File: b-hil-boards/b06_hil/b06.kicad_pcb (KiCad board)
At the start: 2 copper layers, 100 x 50 mm, 22 parts, among them J1 Conn_01x08_Socket, J3 USB_C_Receptacle_PowerOnly_6P, SW1 SW_Push, U4 ESP32_C3_SuperMini, U5 OLED-128x64-I2C

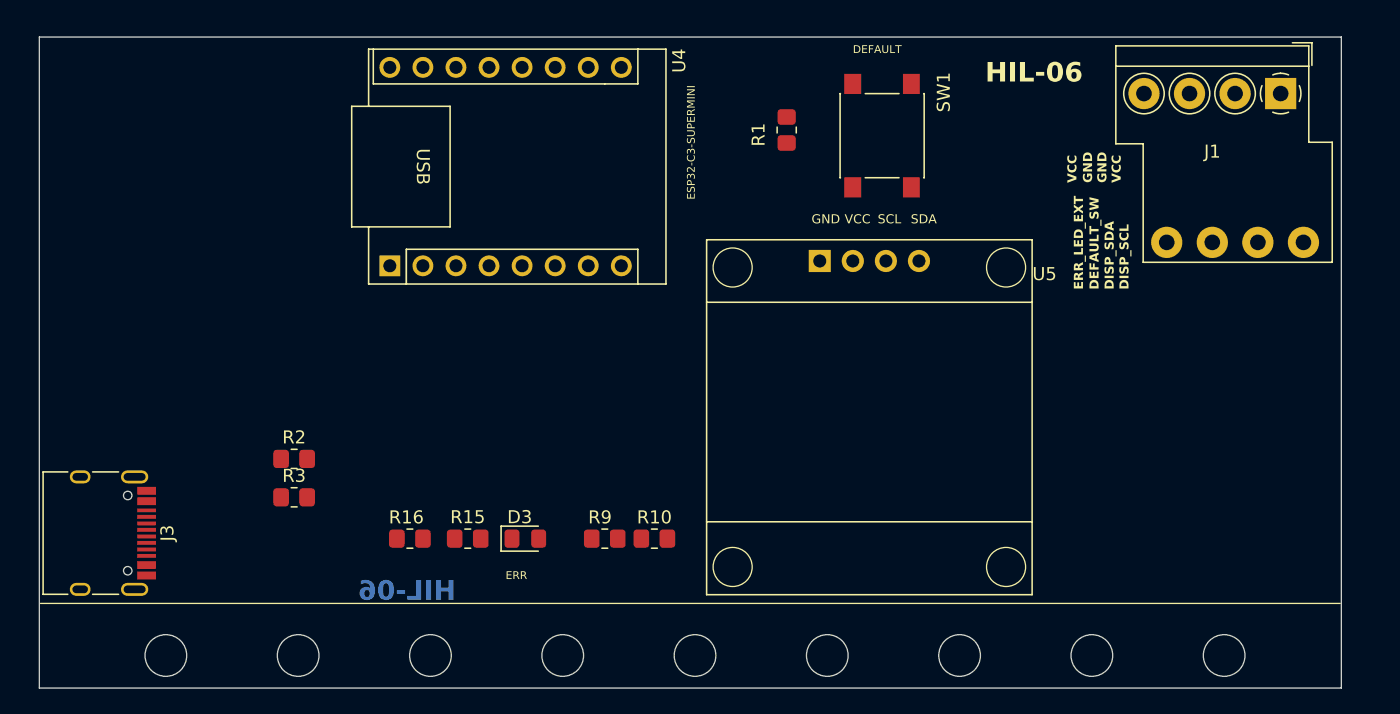
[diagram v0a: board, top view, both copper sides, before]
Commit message: B06: finalize PCB routing and design data
Complete the routed layout in b06.kicad_pcb, align schematic and project
settings, refresh fp-info-cache and sym-lib-table, add FreeRouting exchange
files (b06.dsn, b06.rules, b06.ses), the INA219 datasheet asset, the
Connector_Improved library symbol, and KiCad automatic backup archives.
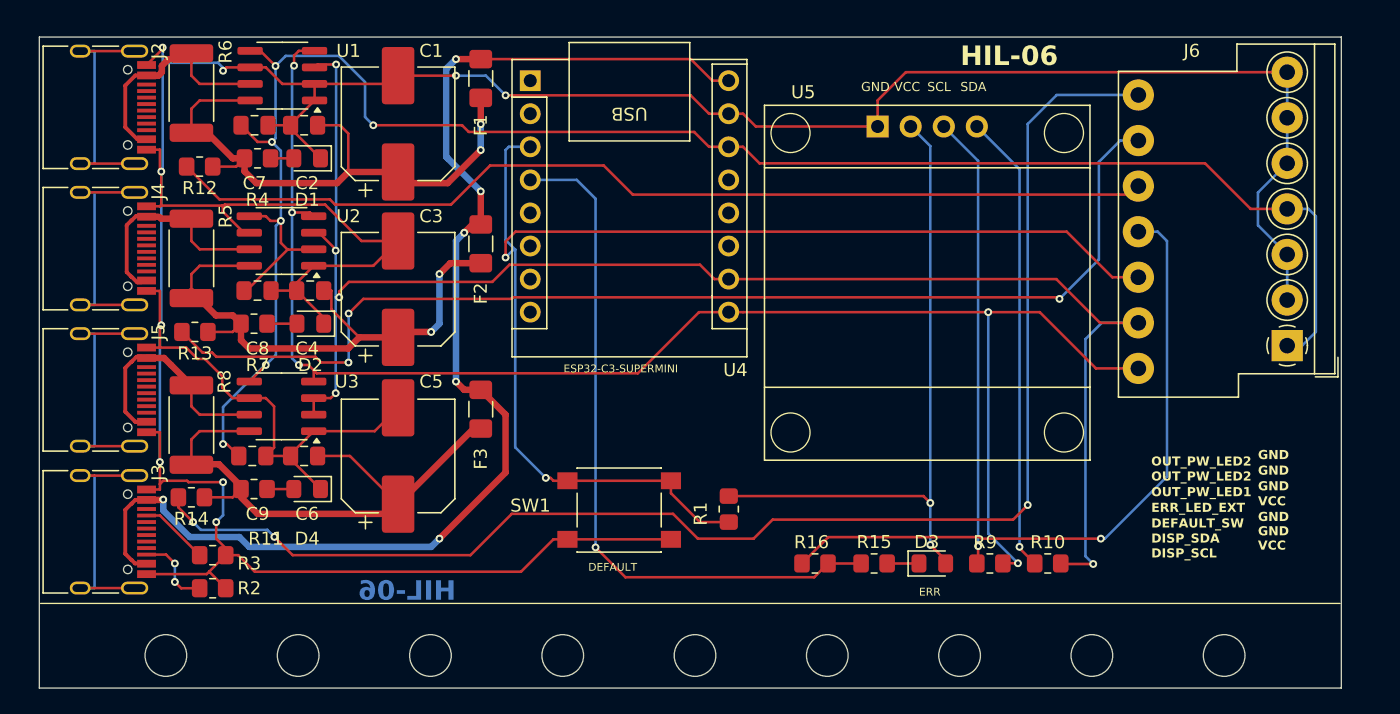
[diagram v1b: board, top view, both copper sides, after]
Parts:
- removed J1: Conn_01x08_Socket, TerminalBlock_DoubleLevel:TerminalBlock_DoubleLevel_2x04_P3.50mm_Horizontal
- added C1: C, Capacitor_SMD:CP_Elec_8x10.5, F.Cu at (107.3, 41.2)
- added C2: C, Capacitor_SMD:C_0805_2012Metric_Pad1.18x1.45mm_HandSolder, F.Cu at (100.1, 41.3)
- added C3: C, Capacitor_SMD:CP_Elec_8x10.5, F.Cu at (107.3, 53.9)
- added C4: C, Capacitor_SMD:C_0805_2012Metric_Pad1.18x1.45mm_HandSolder, F.Cu at (100.6, 54.0)
- added C5: C, Capacitor_SMD:CP_Elec_8x10.5, F.Cu at (107.3, 66.7)
- added C6: C, Capacitor_SMD:C_0805_2012Metric_Pad1.18x1.45mm_HandSolder, F.Cu at (100.1, 66.7)
- added C7: C, Capacitor_SMD:C_0805_2012Metric_Pad1.18x1.45mm_HandSolder, F.Cu at (96.3, 41.3)
- added C8: C, Capacitor_SMD:C_0805_2012Metric_Pad1.18x1.45mm_HandSolder, F.Cu at (96.5, 54.0)
- added C9: C, Capacitor_SMD:C_0805_2012Metric_Pad1.18x1.45mm_HandSolder, F.Cu at (96.1, 66.7)
- added D1: LED, LED_SMD:LED_0805_2012Metric_Pad1.15x1.40mm_HandSolder, F.Cu at (100.3, 43.8)
- added D2: LED, LED_SMD:LED_0805_2012Metric_Pad1.15x1.40mm_HandSolder, F.Cu at (100.6, 56.5)
- added D4: LED, LED_SMD:LED_0805_2012Metric_Pad1.15x1.40mm_HandSolder, F.Cu at (100.3, 69.2)
- added F1: Polyfuse, Fuse:Fuse_1206_3216Metric_Pad1.42x1.75mm_HandSolder, F.Cu at (113.7, 37.7)
- added F2: Polyfuse, Fuse:Fuse_1206_3216Metric_Pad1.42x1.75mm_HandSolder, F.Cu at (113.7, 50.4)
- added F3: Polyfuse, Fuse:Fuse_1206_3216Metric_Pad1.42x1.75mm_HandSolder, F.Cu at (113.7, 63.1)
- added J2: USB_C_Receptacle_PowerOnly_6P_Improved, Connector_USB:USB_C_Receptacle_HRO_TYPE-C-31-M-12, F.Cu at (84.0, 39.9)
- added J4: USB_C_Receptacle_PowerOnly_6P_Improved, Connector_USB:USB_C_Receptacle_HRO_TYPE-C-31-M-12, F.Cu at (84.0, 50.8)
- added J5: USB_C_Receptacle_PowerOnly_6P_Improved, Connector_USB:USB_C_Receptacle_HRO_TYPE-C-31-M-12, F.Cu at (84.0, 61.6)
- added J6: Conn_01x14_Socket, TerminalBlock_DoubleLevel:TerminalBlock_DoubleLevel_2x07_P3.50mm_Horizontal, F.Cu at (175.6, 58.2)
- added R11: R, Resistor_SMD:R_0805_2012Metric_Pad1.20x1.40mm_HandSolder, F.Cu at (96.2, 69.2)
- added R12: R, Resistor_SMD:R_0805_2012Metric_Pad1.20x1.40mm_HandSolder, F.Cu at (92.1, 44.5)
- added R13: R, Resistor_SMD:R_0805_2012Metric_Pad1.20x1.40mm_HandSolder, F.Cu at (91.7, 57.1)
- added R14: R, Resistor_SMD:R_0805_2012Metric_Pad1.20x1.40mm_HandSolder, F.Cu at (91.4, 69.8)
- added R4: R, Resistor_SMD:R_0805_2012Metric_Pad1.20x1.40mm_HandSolder, F.Cu at (96.5, 43.8)
- added R5: R, Resistor_SMD:R_2512_6332Metric_Pad1.40x3.35mm_HandSolder, F.Cu at (91.4, 51.5)
- added R6: R, Resistor_SMD:R_2512_6332Metric_Pad1.40x3.35mm_HandSolder, F.Cu at (91.4, 38.8)
- added R7: R, Resistor_SMD:R_0805_2012Metric_Pad1.20x1.40mm_HandSolder, F.Cu at (96.2, 56.5)
- added R8: R, Resistor_SMD:R_2512_6332Metric_Pad1.40x3.35mm_HandSolder, F.Cu at (91.4, 64.3)
- added U1: INA219AxD, Package_SO:SOIC-8_3.9x4.9mm_P1.27mm, F.Cu at (98.4, 37.5)
- added U2: INA219AxD, Package_SO:SOIC-8_3.9x4.9mm_P1.27mm, F.Cu at (98.4, 50.2)
- added U3: INA219AxD, Package_SO:SOIC-8_3.9x4.9mm_P1.27mm, F.Cu at (98.4, 62.9)
- J3: value USB_C_Receptacle_PowerOnly_6P -> USB_C_Receptacle_PowerOnly_6P_Improved
- moved SW1 35.1 mm to (124.3, 70.8), turned to 0 degrees
- moved D3 31.3 mm to (148.3, 74.9)
- moved R15 31.3 mm to (143.9, 74.9)
- moved R16 31.2 mm to (139.3, 74.9)
- moved R10 30.3 mm to (157.2, 74.9)
- moved R9 29.6 mm to (152.8, 74.9)
- moved R1 29.5 mm to (132.7, 70.8)
- moved U4 17.8 mm to (117.5, 37.9), turned to 180 degrees
- moved R2 11.7 mm to (93.1, 76.8)
- moved U5 11.2 mm to (144.1, 41.4)
- moved R3 7.67 mm to (93.1, 74.3)
- moved J3 0.10 mm to (84.0, 72.5)
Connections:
- J3 pad A1: (no net) -> GND
- J3 pad A12: GND1 -> GND
- J3 pad A4: (no net) -> +5V
- J3 pad B1: (no net) -> GND
- J3 pad B12: GND1 -> GND
- J3 pad B4: (no net) -> +5V
- R2 pad 2: GND1 -> GND
- R3 pad 2: GND1 -> GND
- SW1 pad 2: GND1 -> GND
- U4 pad 14: unconnected-(U4-3V3-Pad14) -> +3.3V
- U4 pad 15: GND1 -> GND
- U5 pad 1: GND1 -> GND
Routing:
- net GND: track 0.00 -> 298.0 mm, vias 0 -> 9
- net +3.3V: track 0.00 -> 150.4 mm, vias 0 -> 6
- net /DISP_SDA: track 0.00 -> 121.8 mm, vias 0 -> 5
- net /DISP_SCL: track 0.00 -> 118.8 mm, vias 0 -> 5
- net /OUT_PW_LED3: track 0.00 -> 109.5 mm, vias 0 -> 3
- net /DEFAULTS: track 0.00 -> 97.1 mm, vias 0 -> 2
- net +5V: track 0.00 -> 97.0 mm, vias 0 -> 6
- net /OUT_PW_LED2: track 0.00 -> 88.2 mm, vias 0 -> 3
- net /OUT_PW_LED1: track 0.00 -> 76.7 mm
- net /ERR_LED: track 0.00 -> 54.2 mm, vias 0 -> 1
- net /ERR_LED_EXT: track 0.00 -> 51.5 mm, vias 0 -> 1
- net +3V3: track 0.00 -> 50.4 mm, vias 0 -> 2
- net Net-(U2-IN+): track 0.00 -> 45.7 mm, vias 0 -> 2
- net Net-(U1-IN+): track 0.00 -> 45.0 mm, vias 0 -> 2
- net Net-(U3-IN+): track 0.00 -> 43.2 mm
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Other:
- board text added: "OUT_PW_LED1"
- board text added: "OUT_PW_LED2"
- board text added: "OUT_PW_LED3"

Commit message: B06: add single-board Gerber outputs
Export gerber/single (copper, mask, paste, silkscreen, edge cuts, drills, and b06-single.zip) for one-up fabrication; refresh PCB, schematic, and project layout; rotate KiCad automatic backups.
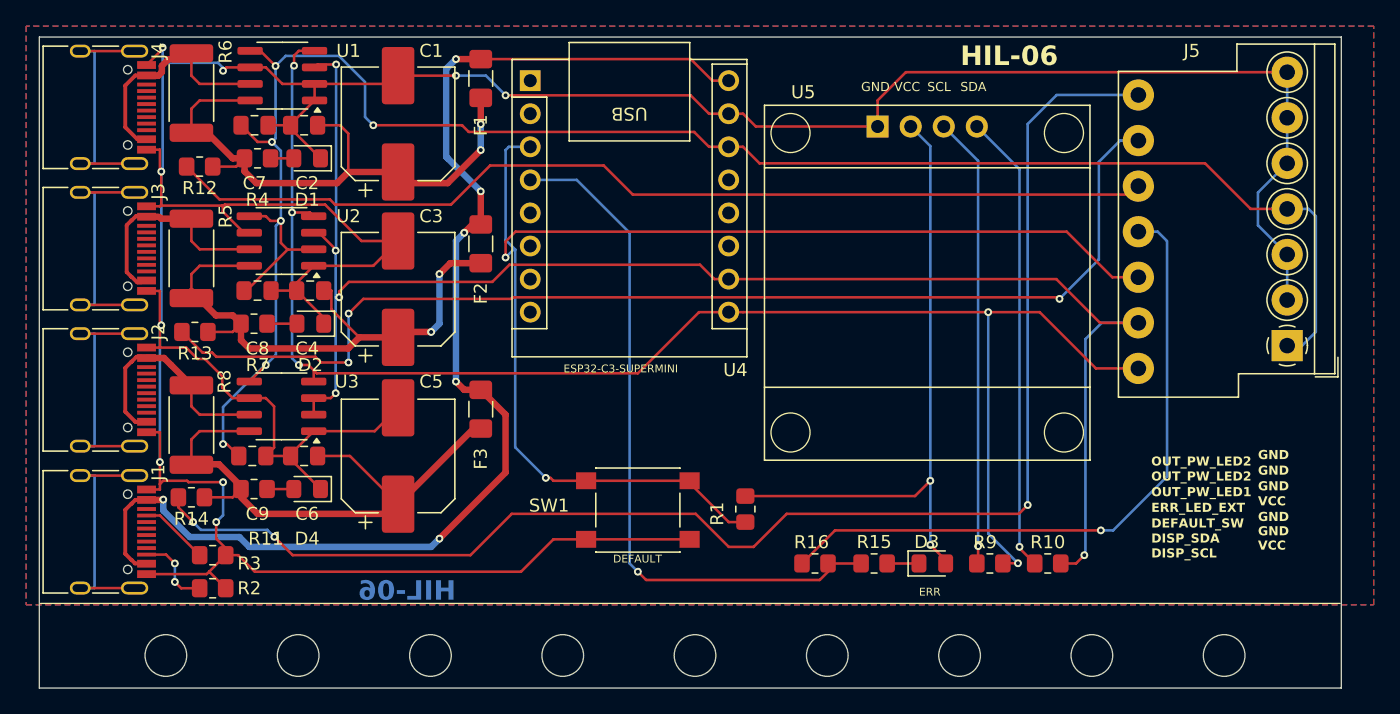
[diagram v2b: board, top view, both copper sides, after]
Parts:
- moved SW1 1.44 mm to (125.7, 70.8)
- moved R1 1.27 mm to (134.0, 70.8)
- renumbered J3 to J1, J5 to J2, J4 to J3, J2 to J4, J6 to J5
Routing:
- net GND: track 298.0 -> 299.5 mm
- net /DISP_SDA: track 121.8 -> 120.5 mm
- net +3V3: track 50.4 -> 49.4 mm
- net /DEFAULTS: track 97.1 -> 97.9 mm
- net /OUT_PW_LED3: track 109.5 -> 110.1 mm
- added copper zone on B.Cu, net GND
- added copper zone on F.Cu, net GND
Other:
- board text added: "OUT 1"
- board text added: "OUT 2"
- board text added: "OUT 3"
- board text added: "POWER INPUT"
